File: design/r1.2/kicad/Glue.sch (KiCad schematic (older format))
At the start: 34 parts, among them IC2 ATF16V8BQL-15PU, IC3 ATF16V8BQL-15PU, IC5 ATF16V8BQL-15PU, IC6 74174N, IC7 74LS93, IC8 555N, IC9 74LS01N, Q2 5H8ET-10.000, Q3 5H8ET-4.000

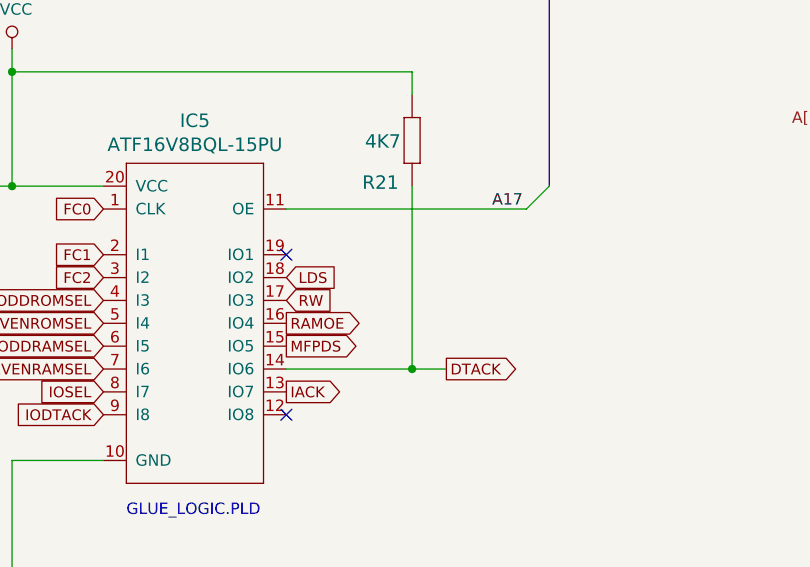
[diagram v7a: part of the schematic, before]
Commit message: Board changes for new DTACK
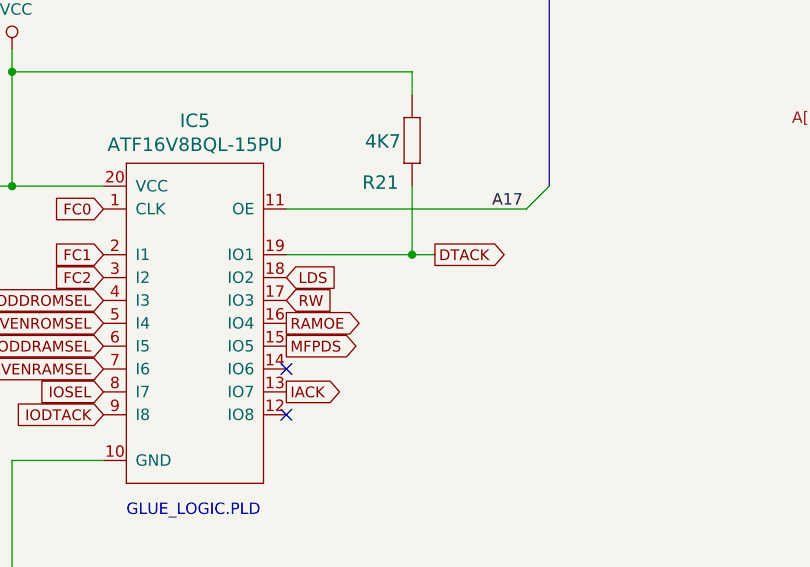
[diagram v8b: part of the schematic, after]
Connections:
- net DTACK: now also IC5.19 (IO1); no longer IC5.14 (IO6)
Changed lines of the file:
@@
 Text GLabel 10300 3800 2    47   Output ~ 0
 IACK
-Text GLabel 11000 3700 2    47   Output ~ 0
+Text GLabel 10950 3200 2    47   Output ~ 0
 DTACK
 Text GLabel 10300 3600 2    47   Output ~ 0
@@
 Wire Wire Line
 	18700 7800 18700 7950
-NoConn ~ 10300 3200
 Wire Wire Line
 	12800 9000 14750 9000
@@
 Wire Wire Line
 	14750 9000 15850 9000
-Wire Wire Line
-	11000 3700 10850 3700
 $Comp
 L rosco_m68k-eagle-import:R-EU_0207_10 R?
@@
 	9100 2400 9100 2900
 Wire Wire Line
-	10850 2900 10850 3700
-Connection ~ 10850 3700
-Wire Wire Line
-	10850 3700 10300 3700
+	10850 2900 10850 3200
 $Comp
 L 74xx:74LS93 IC7
@@
 A17
 Wire Wire Line
+	10300 3200 10850 3200
+Wire Wire Line
+	10950 3200 10850 3200
+Connection ~ 10850 3200
+NoConn ~ 10300 3700
+Wire Wire Line
 	18700 6600 19700 6600
